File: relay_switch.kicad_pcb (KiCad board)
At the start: 2 copper layers, 25.7 x 64.6 mm, 20 parts, among them P1 board_mount, P10 INPUT2, P11 INPUT3, P12 INPUT4, P13 POWER, P14 J_CONN_01X04, P2 board_mount, P3 board_mount, P4 board_mount, P8 OUTPUT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

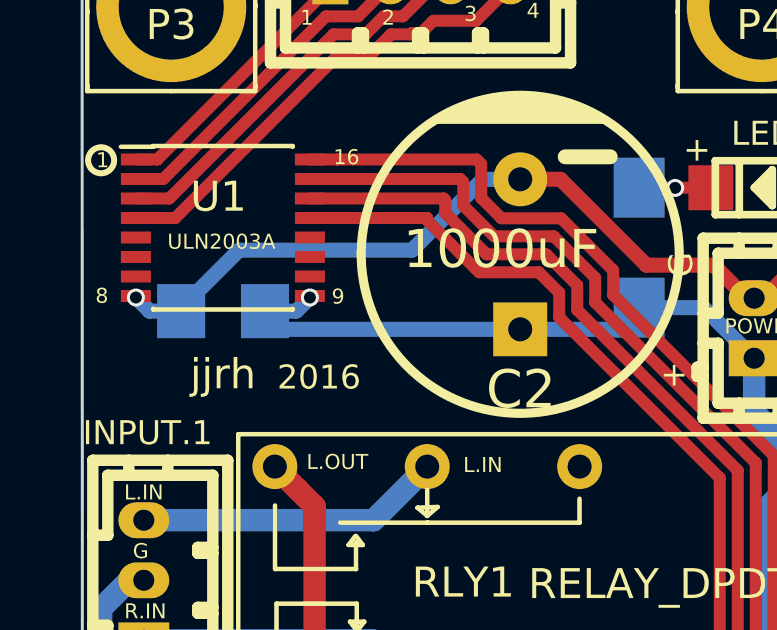
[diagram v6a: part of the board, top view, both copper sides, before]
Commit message: moved vias for cap so they weren't ontop of the pads
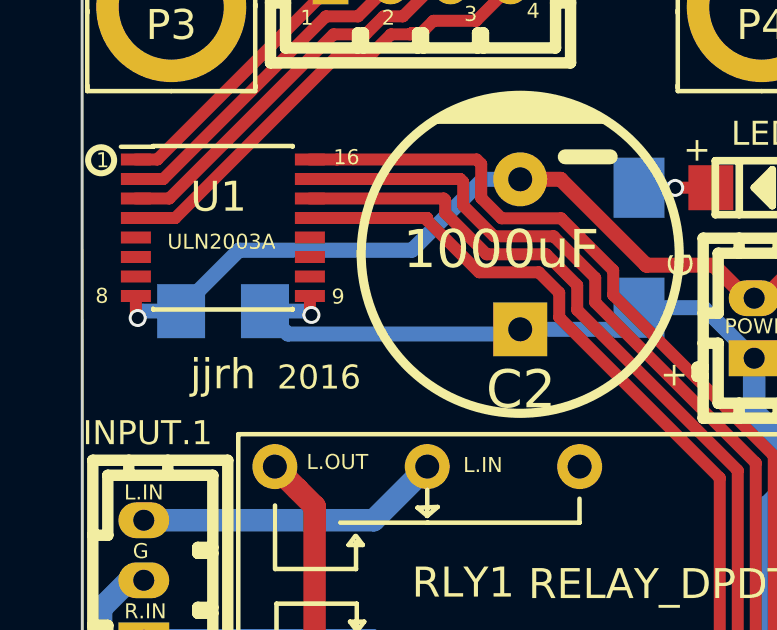
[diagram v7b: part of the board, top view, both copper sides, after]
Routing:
- net +12V: track 58.4 -> 59.1 mm
- net GND: track 29.1 -> 29.7 mm
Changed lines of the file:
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@@
   (general
     (links 41)
-    (no_connects 16)
-    (area 122.2166 96.74164 174.911868 178.034541)
+    (no_connects 0)
+    (area 131.471199 104.191599 157.225201 168.909462)
     (thickness 1.6)
     (drawings 130)
-    (tracks 201)
+    (tracks 208)
     (zones 0)
     (modules 20)
@@
   )
   (setup
-    (last_trace_width 0.5)
+    (last_trace_width 0.4)
     (user_trace_width 0.25)
     (user_trace_width 0.4)
@@
   (gr_line (start 131.5212 104.2416) (end 131.5466 168.8592) (layer Edge.Cuts) (width 0.1))
   (gr_line (start 157.1498 104.2416) (end 131.5212 104.2416) (layer Edge.Cuts) (width 0.1))
+  (segment (start 133.3158 117.4916) (end 133.3754 117.5512) (width 0.4) (layer F.Cu) (net 1))
+  (segment (start 133.3158 116.818) (end 133.3158 117.4916) (width 0.4) (layer F.Cu) (net 1))
+  (segment (start 133.5231 117.3226) (end 133.3754 117.4703) (width 0.5) (layer B.Cu) (net 1))
+  (segment (start 134.8232 117.3226) (end 133.5231 117.3226) (width 0.5) (layer B.Cu) (net 1))
+  (segment (start 133.3754 117.4703) (end 133.3754 117.5512) (width 0.5) (layer B.Cu) (net 1))
+  (via (at 133.3754 117.5512) (size 0.6) (drill 0.4) (layers F.Cu B.Cu) (net 1))
   (segment (start 134.8232 117.3226) (end 134.8232 117.221) (width 0.5) (layer B.Cu) (net 1))
   (segment (start 134.8232 117.221) (end 136.7536 115.2906) (width 0.5) (layer B.Cu) (net 1))
@@
   (segment (start 155.97632 115.08867) (end 154.17419 116.8908) (width 0.4) (layer F.Cu) (net 1))
   (segment (start 154.17419 116.8908) (end 153.924 116.8908) (width 0.4) (layer F.Cu) (net 1))
-  (segment (start 134.8232 117.3226) (end 133.770398 117.3226) (width 0.5) (layer B.Cu) (net 1))
-  (segment (start 133.770398 117.3226) (end 133.3158 116.868002) (width 0.5) (layer B.Cu) (net 1))
-  (via (at 133.3158 116.868002) (size 0.6) (drill 0.4) (layers F.Cu B.Cu) (net 1))
   (segment (start 153.8732 116.9416) (end 153.924 116.8908) (width 0.25) (layer F.Cu) (net 1))
   (segment (start 140.838577 164.282777) (end 142.1384 165.5826) (width 0.75) (layer F.Cu) (net 2))
@@
   (segment (start 139.90934 156.0322) (end 135.12743 156.0322) (width 0.75) (layer B.Cu) (net 11))
   (segment (start 135.12743 156.0322) (end 133.5278 156.0322) (width 0.75) (layer B.Cu) (net 11))
-  (segment (start 137.6172 117.3226) (end 138.661202 117.3226) (width 0.5) (layer B.Cu) (net 12))
-  (segment (start 138.661202 117.3226) (end 139.1158 116.868002) (width 0.5) (layer B.Cu) (net 12))
-  (via (at 139.1158 116.868002) (size 0.6) (drill 0.4) (layers F.Cu B.Cu) (net 12))
-  (segment (start 146.1262 117.9284) (end 138.223 117.9284) (width 0.5) (layer B.Cu) (net 12))
-  (segment (start 138.223 117.9284) (end 137.6172 117.3226) (width 0.5) (layer B.Cu) (net 12))
+  (segment (start 139.0396 117.3226) (end 139.1666 117.4496) (width 0.5) (layer B.Cu) (net 12))
+  (segment (start 137.6172 117.3226) (end 139.0396 117.3226) (width 0.5) (layer B.Cu) (net 12))
+  (segment (start 139.1474 117.4496) (end 139.1666 117.4496) (width 0.4) (layer F.Cu) (net 12))
+  (segment (start 139.1158 117.418) (end 139.1474 117.4496) (width 0.4) (layer F.Cu) (net 12))
+  (segment (start 139.1158 116.818) (end 139.1158 117.418) (width 0.4) (layer F.Cu) (net 12))
+  (via (at 139.1666 117.4496) (size 0.6) (drill 0.4) (layers F.Cu B.Cu) (net 12))
+  (segment (start 146.1262 117.9284) (end 145.97 118.0846) (width 0.5) (layer B.Cu) (net 12))
+  (segment (start 145.97 118.0846) (end 138.3792 118.0846) (width 0.5) (layer B.Cu) (net 12))
+  (segment (start 138.3792 118.0846) (end 137.6172 117.3226) (width 0.5) (layer B.Cu) (net 12))
   (segment (start 150.0886 117.2078) (end 152.23948 117.2078) (width 0.5) (layer B.Cu) (net 12))
   (segment (start 152.23948 117.2078) (end 153.924 118.89232) (width 0.5) (layer B.Cu) (net 12))
